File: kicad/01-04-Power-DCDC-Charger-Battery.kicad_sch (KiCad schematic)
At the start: 63 parts, among them J3 S2B-PH-K-S_LF__SN_, Q1 PMOS, Q2 AO3400A, Q3 AO3400A, U2 MCP73831-2-OT, U3 BQ29700DSER, U4 TLV62568DBVR

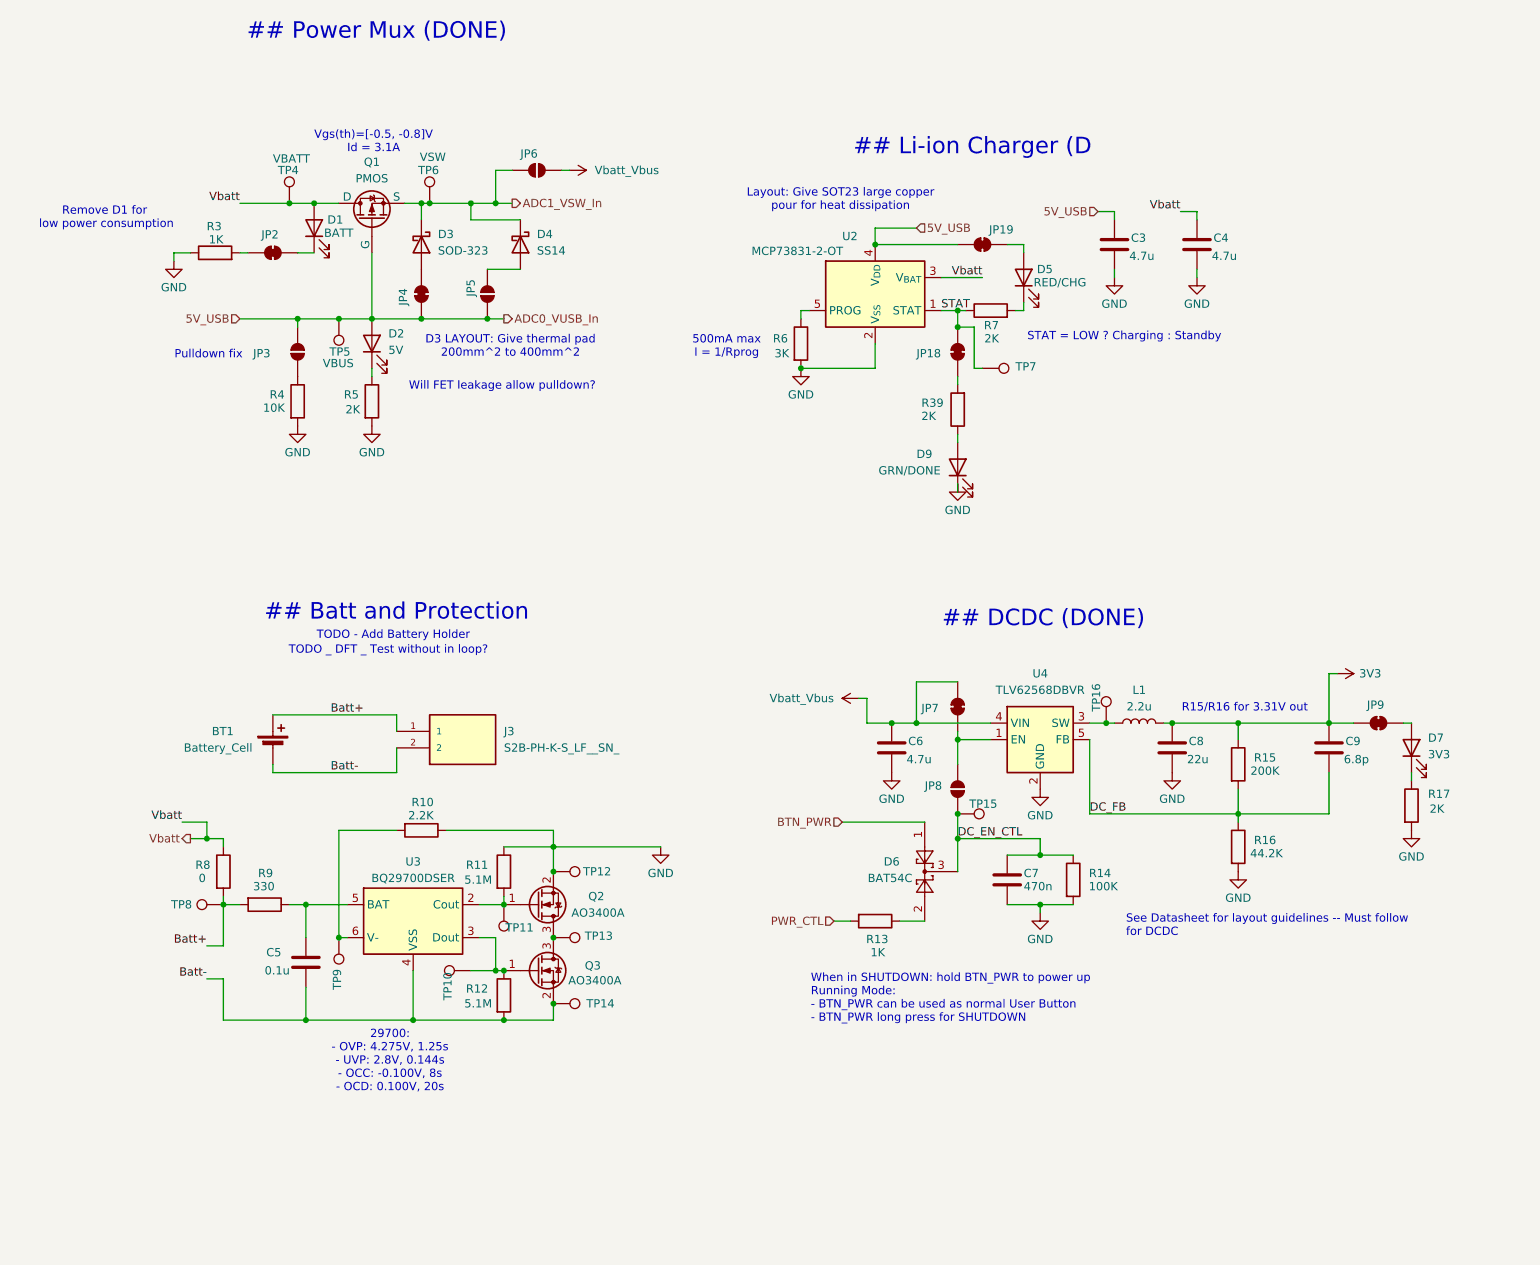
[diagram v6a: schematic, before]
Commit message: charger pcb update
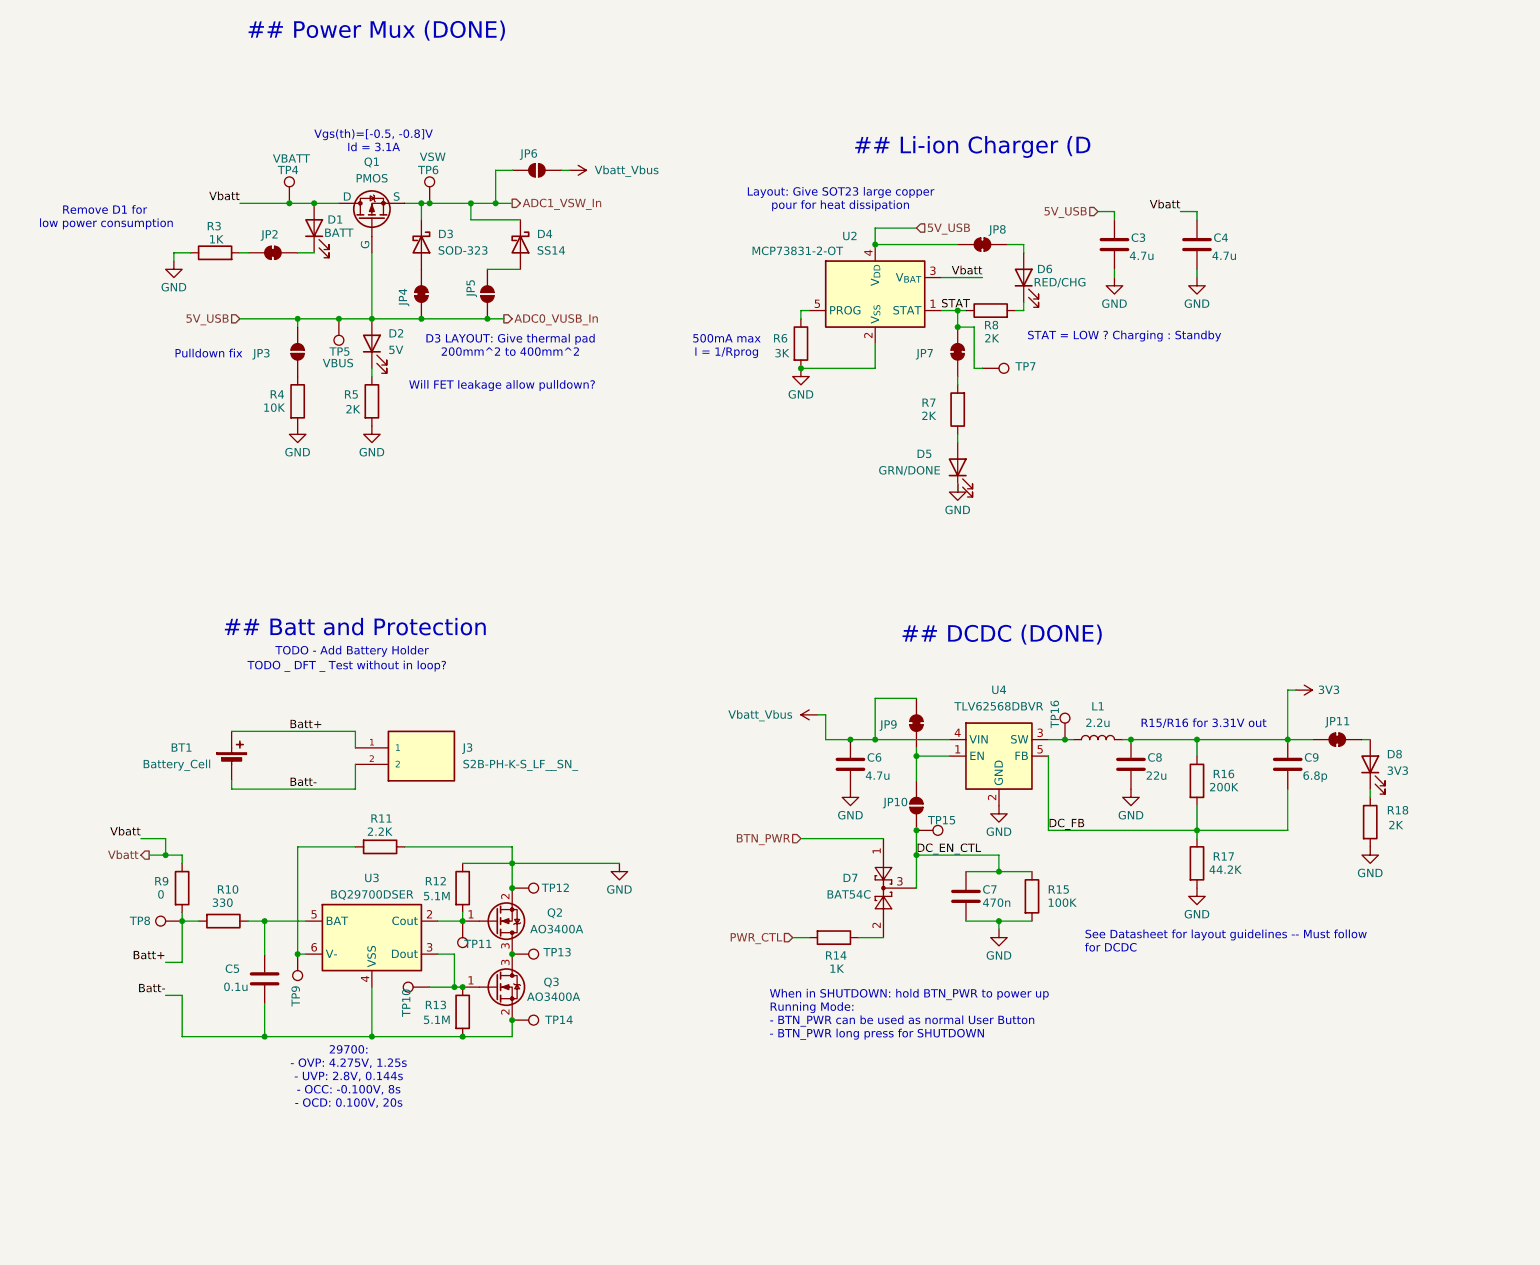
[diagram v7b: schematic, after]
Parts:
- renumbered D9 to D5, D5 to D6, D6 to D7, D7 to D8, JP8 to JP10, JP9 to JP11, JP18 to JP7, JP19 to JP8, JP7 to JP9, R9 to R10, R10 to R11, R11 to R12, R12 to R13, R13 to R14, R14 to R15, R15 to R16, R16 to R17, R17 to R18, R39 to R7, R7 to R8, R8 to R9
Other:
- moved on the sheet: BT1, C5, C6, C7, C8, C9, D7, D8, J3, JP10, JP11, JP9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

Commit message: DR SYS-04-Battery Protect ✅
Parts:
- added BOM1: JST PH 2.0mm Connector Kit, symbol Project_Library:BOM_PLACEHOLDER
- added BOM2: Crimp Pliers for JST-PH connectors, symbol Project_Library:BOM_PLACEHOLDER
- added JP10: SolderJumper_2_Open, Jumper:SolderJumper-2_P1.3mm_Open_RoundedPad1.0x1.5mm, symbol Jumper:SolderJumper_2_Open
- added JP9: SolderJumper_2_Bridged, Jumper:SolderJumper-2_P1.3mm_Bridged_RoundedPad1.0x1.5mm, symbol Jumper:SolderJumper_2_Bridged
- added TP9: BAT-, project footprints:TestPoint_THTPad_D2.0mm_Drill1.0mm, symbol Connector:TestPoint
- BT1, R10, R11, R12, R13, R9: MPN (none) -> (Generic); Manufacturer (none) -> (Generic); Subsystem (none) -> 04-Batt-Prot; Supplier 1 (none) -> (Generic)
- C5: footprint (none) -> Capacitor_SMD:C_0805_2012Metric_Pad1.18x1.45mm_HandSolder; MPN (none) -> (Generic); Manufacturer (none) -> (Generic); Package (none) -> 0805; Subsystem (none) -> 04-Batt-Prot; Supplier 1 (none) -> (Generic)
- J3: MPN (none) -> S2B-PH-K-S; Manufacturer (none) -> JST; Subsystem (none) -> 04-Batt-Prot; Supplier 1 (none) -> Digikey; Supplier 1 URL (none) -> https://www.digikey.jp/en/products/detail/jst-sales-america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
- Q2, Q3: MPN (none) -> AO3400A; Manufacturer (none) -> Alpha & Omega Semicon; Package (none) -> SOT-23; Subsystem (none) -> 04-Batt-Prot; Supplier 1 (none) -> LCSC; Supplier 1 SKU (none) -> C20917; Supplier 1 URL (none) -> https://jlcpcb.com/partdetail/Alpha_OmegaSemicon-AO3400A/C2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
- R3: MPN (none) -> (Generic)
- TP10: renamed from TP9; value TestPoint -> U3_V-; Subsystem (none) -> 04-Batt-Prot
- TP11: renamed from TP10; value TestPoint -> DSG; Subsystem (none) -> 04-Batt-Prot
- TP12: renamed from TP11; value TestPoint -> CHG
- TP13: renamed from TP12; value TestPoint -> GND; Subsystem (none) -> 04-Batt-Prot
- TP14: renamed from TP13; value TestPoint -> Q23_D; Subsystem (none) -> 04-Batt-Prot
- TP15: renamed from TP14; value TestPoint -> BAT-; Subsystem (none) -> 04-Batt-Prot
- TP8: value TestPoint -> BAT+; Subsystem (none) -> 04-Batt-Prot
- U3: Subsystem (none) -> 04-Batt-Prot
- renumbered JP9 to JP11, JP10 to JP12, JP11 to JP13, TP15 to TP16, TP16 to TP17
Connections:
- net Batt-: now also JP9.1 (A), TP9.1
- net GND: now also JP9.2 (B)
- net at C5.1, R10.1: now also JP10.2 (B); no longer U3.5 (BAT)
- new net: JP10.1 (A), U3.5 (BAT)
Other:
- note added: "## Batt and Protection (DONE)"
- note added: "BQ29700: - OVP: 4.275V, 1.25s - UVP: 2.8V, 0.144s - OCC: -0.100V, 8s - OCD: 0.100V, 20s"
- note added: "Bypass U3: JP9 CLOSE & JP10 OPEN"
- note added: "Depending on routing"
- note added: "Rsense"
- note added: "TODO/v2: Integrated dual channel NMOS"
- note added: "TODO/v2: Update to smaller connector"
- note added: "TODO/v2: battery form factor see Adafruit 3898"
- note removed: "## Batt and Protection"
- note removed: "29700: - OVP: 4.275V, 1.25s - UVP: 2.8V, 0.144s - OCC: -0.100V, 8s - OCD: 0.100V, 20s"
- note removed: "TODO - Add Battery Holder"
- moved on the sheet: BT1, C5, C6, C7, C8, C9, D7, D8, J3, JP11, JP12, JP13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
